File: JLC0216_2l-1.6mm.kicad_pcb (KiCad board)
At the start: 2 copper layers, 24 x 24 mm, 3 parts

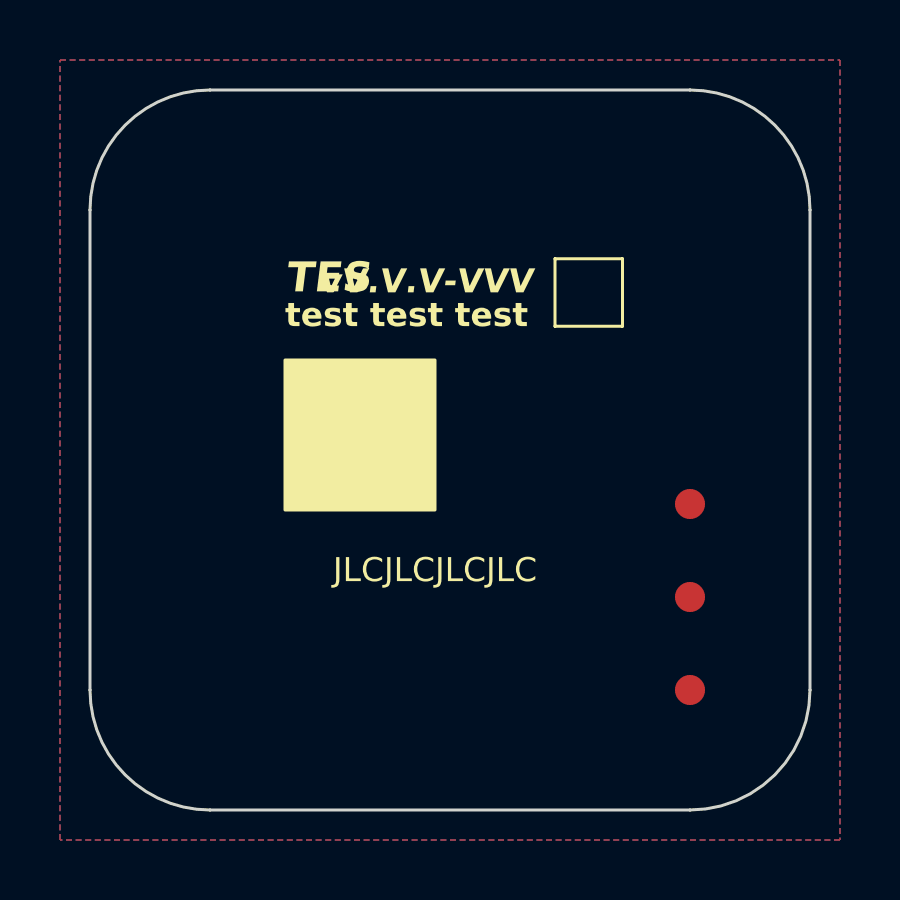
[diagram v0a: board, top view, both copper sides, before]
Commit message: Remove JLCJLCJLCJLC silkscreen text from board layouts
Co-Authored-By: Claude Sonnet 5 <noreply@anthropic.com>
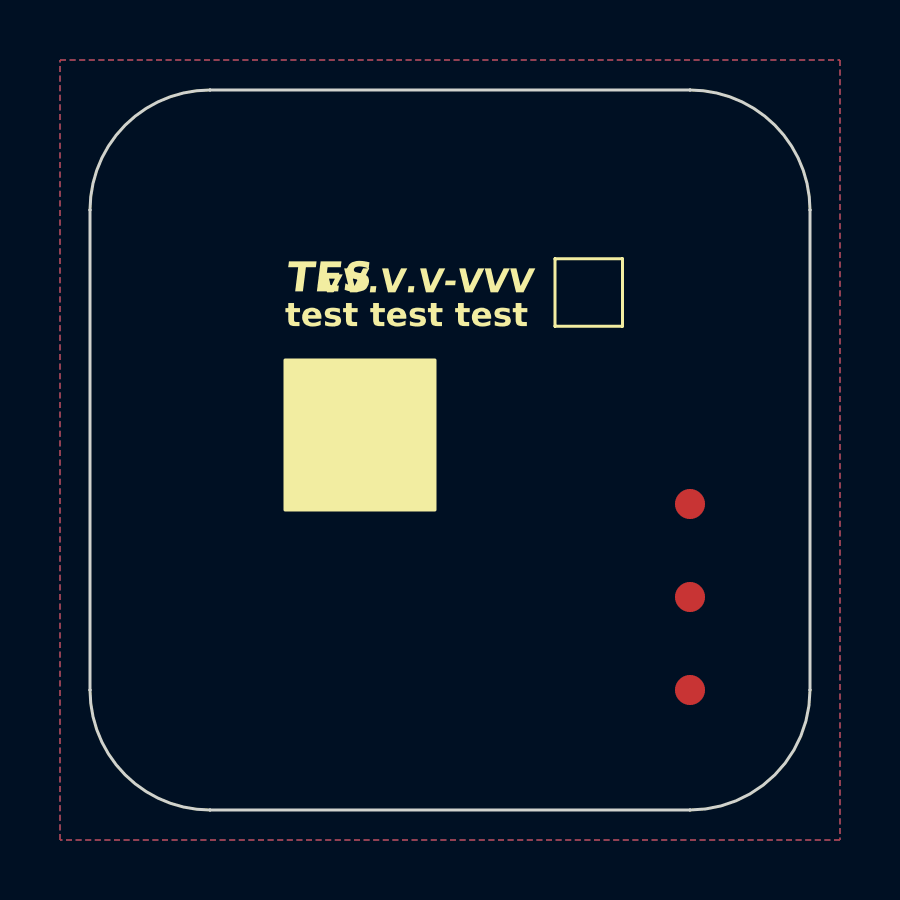
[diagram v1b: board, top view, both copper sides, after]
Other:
- board text removed: "JLCJLCJLCJLC"
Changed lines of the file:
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@@
-		)
-	)
-	(gr_text "JLCJLCJLCJLC"
-		(at 41.5 46 0)
-		(layer "F.SilkS")
-		(effects
-			(font
-				(size 0.8 0.8)
-				(thickness 0.15)
-			)
 		)
 	)
